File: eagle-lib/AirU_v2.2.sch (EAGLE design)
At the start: 86 parts, among them Q1 BSS138W-7-F, Q2 MMBT3904LT1G, Q3 MMBT3904LT1G, Q5 NCE3407A, U1 HDC1080DMBT, U2 CH340T-SSOP20, U3 CJT1117-3.3-SOT223, U4 MAX2659-DFN6, U5 L70-M39, U6 MOLEX-53261-0871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

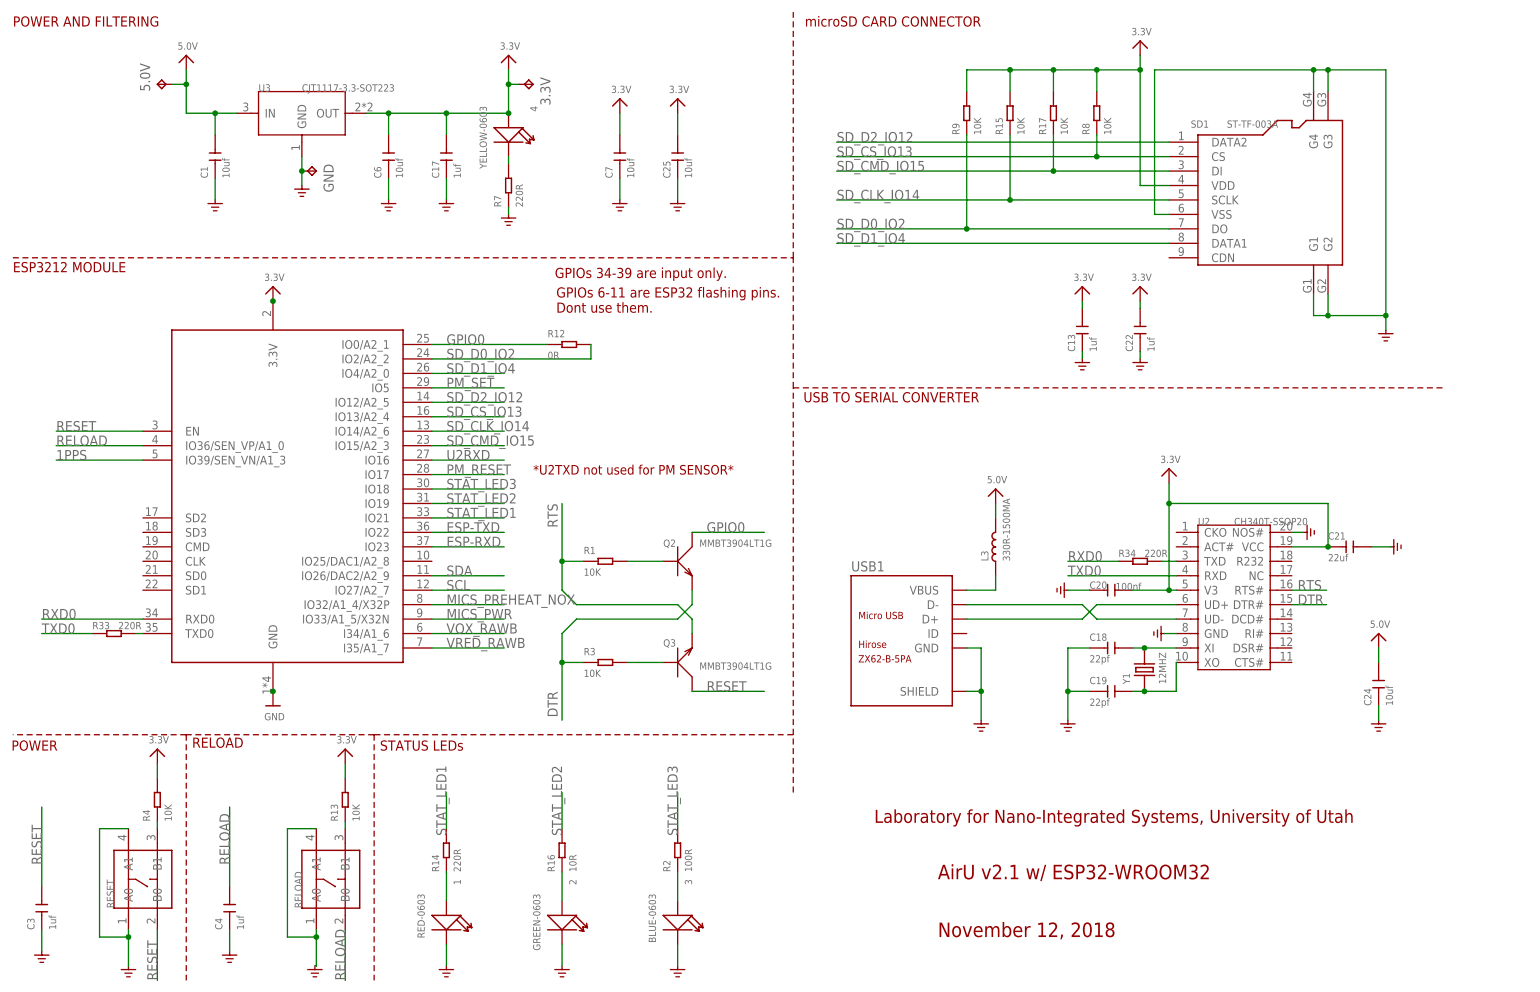
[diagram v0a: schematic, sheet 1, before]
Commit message: board update
PM SET/RESET moved to RTC GPIO pins, MiCS pins swapped to avoid cross-over, sd moved to bottom, usb-uart moved to bottom, gps moved, temp sensor moved to avoid overheating, 5v-3.3v converter moved, 3.3V rail size increased for heat dissipation, tetrad logo added, buttons moved
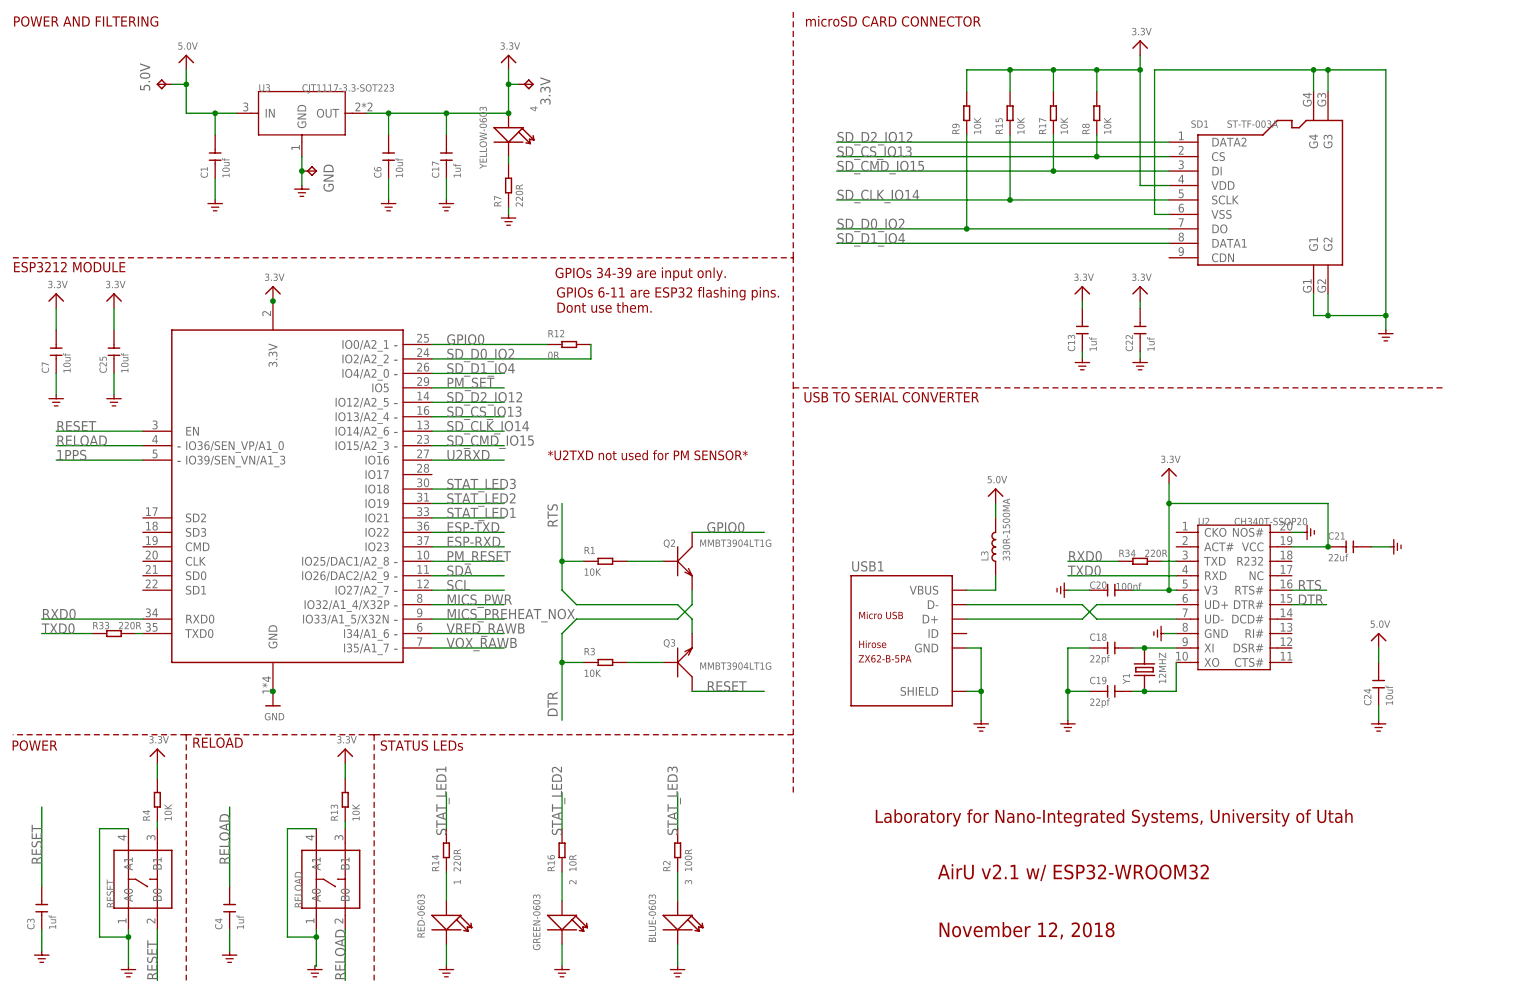
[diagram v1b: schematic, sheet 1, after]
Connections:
- net MICS_PREHEAT_NOX: now also U7.IO33/A1_5/X32N; no longer U7.IO32/A1_4/X32P
- net MICS_PWR: now also U7.IO32/A1_4/X32P; no longer U7.IO33/A1_5/X32N
- net PM_RESET: now also U7.IO25/DAC1/A2_8; no longer U7.IO17
- net VOX_RAWA: now also U8.5; no longer U8.3
- net VOX_RAWB: now also U7.I35/A1_7, U8.6, U8.7; no longer U7.I34/A1_6, U8.1, U8.2
- net VRED_RAWA: now also U8.3; no longer U8.5
- net VRED_RAWB: now also U7.I34/A1_6, U8.1, U8.2; no longer U7.I35/A1_7, U8.6, U8.7
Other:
- note added: "-"
- moved on the sheet: C25, C7
